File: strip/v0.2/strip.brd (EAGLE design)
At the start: 71 x 12 mm, 102 parts, among them IC1 LP2992, IC2 ADP3110A-SO8, IC3 MAX3051, IC4 OPA335, IC5 ADP3110A-SO8, IC6 ADP3110A-SO8, IC7 STM32F050CX, Q1 IRF7828, Q2 IRF7828, Q3 IRF7828, Q4 IRF7828, Q5 IRF7828, Q6 IRF7828

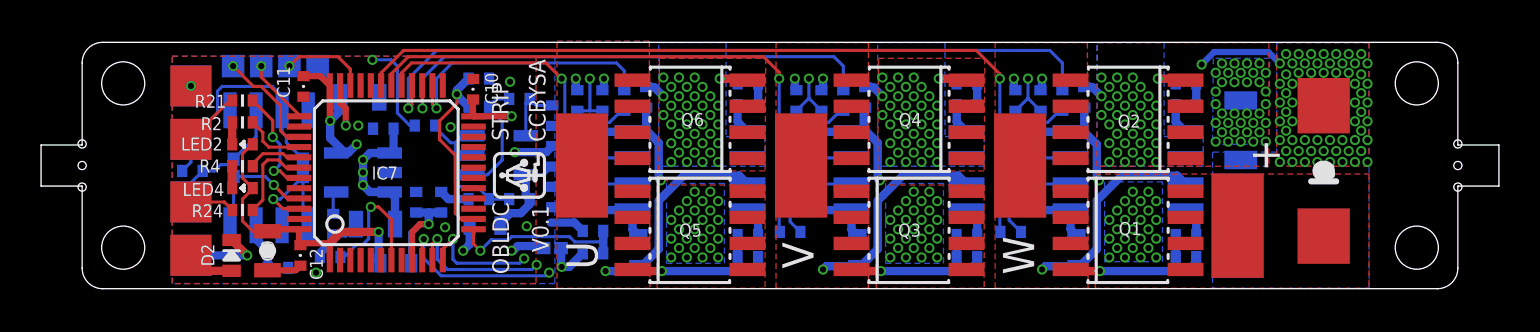
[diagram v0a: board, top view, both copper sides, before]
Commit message: Added new variant of the strip board.
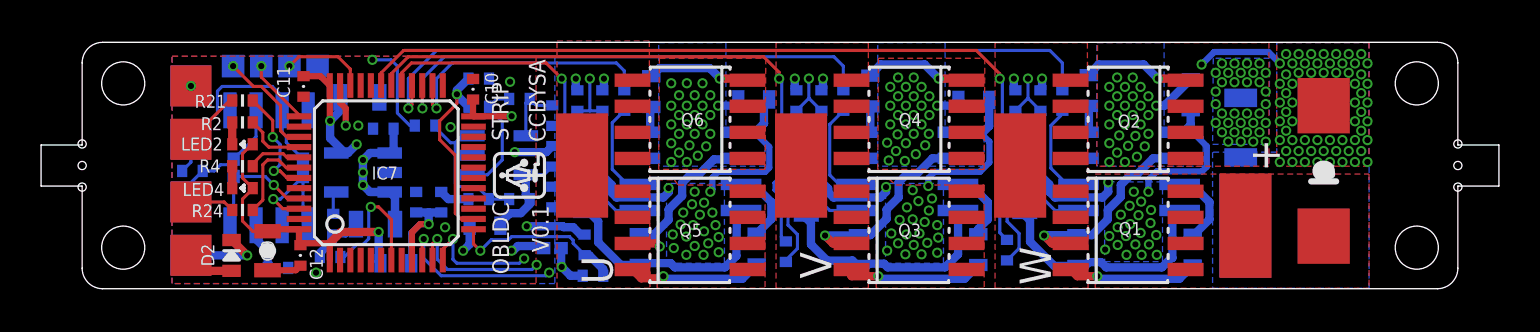
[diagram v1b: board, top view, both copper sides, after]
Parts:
- removed L2, L3, L4, L5, L6, L7: (no value), pel_dipol_comp:0402-IND
- C13: value 100nF -> 100n
- C26, C27, C32: device pel_dipol_comp:0402-CAP -> pel_dipol_comp:0603-CAP
- IC2, IC5, IC6: value ADP3110A-SO8 -> AUIRS2184S; device open-bldc:SO8 -> auris2184s:SOIC127P600X175-8N
- R46, R47, R48, R49, R50, R51: device pel_dipol_comp:0402-RES -> pel_dipol_comp:0603-RES
- moved C27 5.29 mm to (39.4, 9.19), turned to 0 degrees
- moved C26 5.24 mm to (28.7, 9.22), turned to 0 degrees
- moved C32 5.18 mm to (50.0, 9.44)
- moved R47 4.74 mm to (45.0, 9.65), turned to 270 degrees
- moved R51 4.72 mm to (23.7, 9.60), turned to 270 degrees
- moved R49 4.72 mm to (34.4, 9.63), turned to 270 degrees
- moved R12 1.09 mm to (20.9, 0.63)
- moved R6 0.98 mm to (30.3, 1.80), turned to 90 degrees
- moved R7 0.90 mm to (41.0, 1.88), turned to 90 degrees
- moved R13 0.80 mm to (20.5, 2.13), turned to 270 degrees
- moved R48 0.66 mm to (39.6, 1.91), turned to 90 degrees
- moved R50 0.58 mm to (28.9, 1.93), turned to 90 degrees
- moved R46 0.47 mm to (50.1, 1.88), turned to 90 degrees
- moved D3 0.40 mm to (31.3, 5.36)
- moved PAD3 0.38 mm to (52.7, 3.07)
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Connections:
- net N$29 renamed W_GATE_HIGH_T
- net N$30 renamed W_GATE_LOW_T
- net N$31 renamed V_GATE_HIGH_T
- net N$32 renamed V_GATE_LOW_T
- net N$34 renamed U_GATE_HIGH_T
- net N$35 renamed U_GATE_LOW_T
- removed net N$2: C23.P$1, D1.C, IC2.1
- removed net N$23: L2.P$2, R46.P$2
- removed net N$24: L3.P$2, R47.P$2
- removed net N$25: L4.P$2, R48.P$2
- removed net N$26: L5.P$2, R49.P$2
- removed net N$27: L6.P$2, R50.P$2
- removed net N$28: L7.P$2, R51.P$2
- removed net N$7: C24.P$1, D3.C, IC5.1
- removed net N$8: C25.P$1, D4.C, IC6.1
- removed net U_!DIS!1: IC2.3, R8.P$2
- removed net U_PWM1: IC2.2, R5.P$1
- removed net V_!DIS!1: IC5.3, R9.P$2
- removed net V_PWM1: IC5.2, R6.P$1
- removed net W_!DIS1: IC6.3, R10.P$2
- removed net W_PWM1: IC6.2, R7.P$1
- new net U_PWM_IN: IC2.1, R5.P$1
- new net U_SD: IC2.2, R8.P$2
- new net U_VB: C23.P$1, D1.C, IC2.8
- new net V_PWM_IN: IC5.1, R6.P$1
- new net V_SD: IC5.2, R9.P$2
- new net V_VB: C24.P$1, D3.C, IC5.8
- new net W_PWM_IN: IC6.1, R7.P$1
- new net W_SD: IC6.2, R10.P$2
- new net W_VB: C25.P$1, D4.C, IC6.8
- net BUSS+: now also IC2.5, IC5.5, IC6.5; no longer IC2.4, IC5.4, IC6.4
- net PGND: no longer IC2.6, IC5.6, IC6.6
- net PHASE_U: now also IC2.6; no longer IC2.7
- net PHASE_V: now also IC5.6; no longer IC5.7
- net PHASE_W: now also IC6.6; no longer IC6.7
- net U_GATE_HIGH: now also IC2.7, R50.P$2; no longer IC2.8, L6.P$1
- net U_GATE_LOW: now also IC2.4, R51.P$2; no longer IC2.5, L7.P$1
- net V_GATE_HIGH: now also IC5.7, R48.P$2; no longer IC5.8, L4.P$1
- net V_GATE_LOW: now also IC5.4, R49.P$2; no longer IC5.5, L5.P$1
- net W_GATE_HIGH: now also IC6.7, R46.P$2; no longer IC6.8, L2.P$1
- net W_GATE_LOW: now also IC6.4, R47.P$2; no longer IC6.5, L3.P$1
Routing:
- net BUSS+: track 22.4 -> 45.4 mm, vias 82 -> 66
- net W_VB: track 0.00 -> 12.2 mm
- net V_VB: track 0.00 -> 11.9 mm
- net U_VB: track 0.00 -> 11.8 mm
- net W_PWM_IN: track 0.00 -> 7.38 mm
- net U_!DIS!1: track 7.22 -> 0.00 mm
- net W_!DIS1: track 7.22 -> 0.00 mm
- net V_!DIS!1: track 7.20 -> 0.00 mm
- net V_PWM_IN: track 0.00 -> 7.17 mm
- net W_PWM1: track 5.36 -> 0.00 mm
- net V_PWM1: track 5.33 -> 0.00 mm
- net U_PWM_IN: track 0.00 -> 5.05 mm
- net V_SD: track 0.00 -> 4.91 mm
- net U_SD: track 0.00 -> 4.74 mm
- net W_SD: track 0.00 -> 4.70 mm
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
